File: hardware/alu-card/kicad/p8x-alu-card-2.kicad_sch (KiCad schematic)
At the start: 9 parts, among them U10 74HCT181, U11 74HCT182, U12 74HCT157, U13 74HCT157, U14 74HCT157, U15 74HCT157, U16 74HCT244, U17 FLAGS, U18 74HCT260

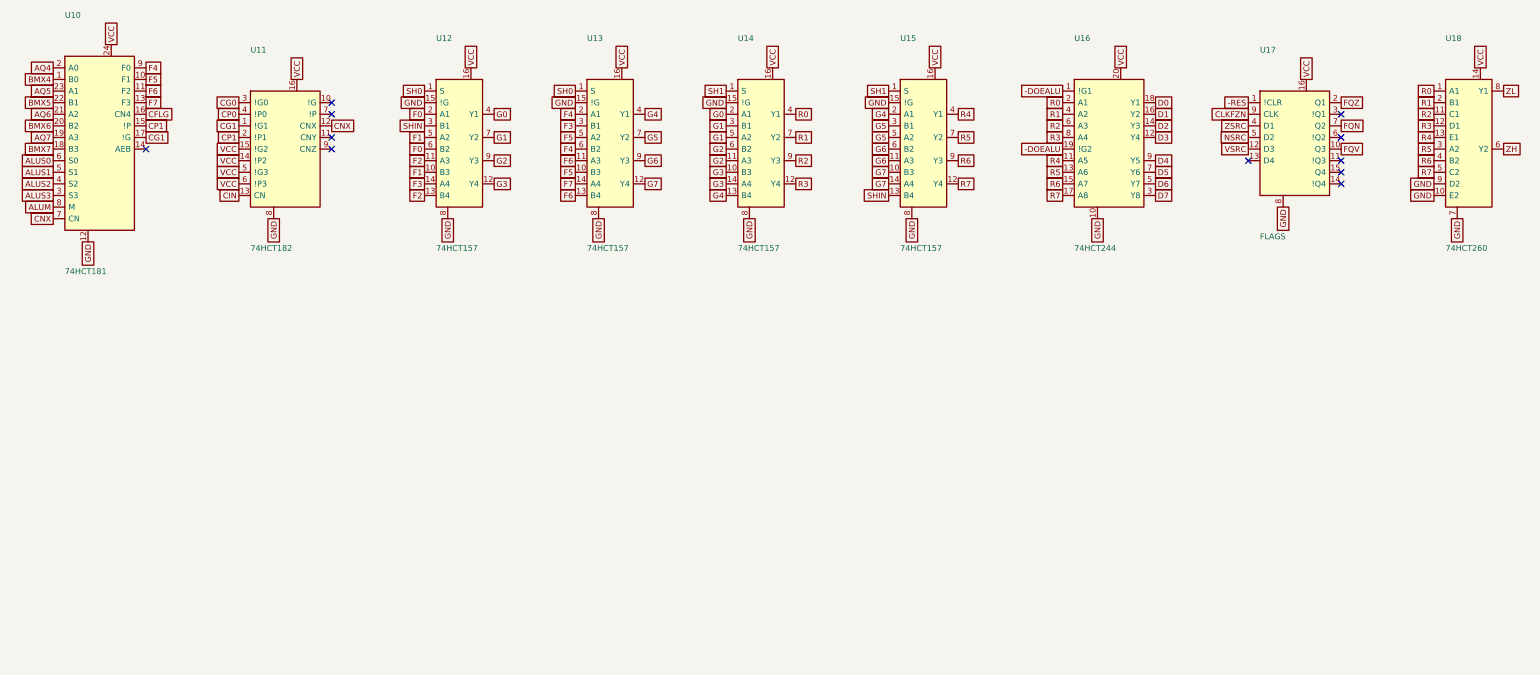
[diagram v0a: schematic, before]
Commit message: feat(sch): draw every P8X card schematic by function
Extend the functional-sheet grouping from the io-card to the control,
regbank, alu, memory, cf, ps2 and bustest cards. functional_sheets now
attaches unnamed glue gates, LEDs, resistors and connectors to the block
they share the most local nets with, so each block lists only its main
parts. A net with two or more pins on a sheet is now wired there even if
it continues elsewhere (its global name label rides on the wire), and
every wire is oriented by drawing side. The regbank gets one pointer per
sheet; the ps2 latches share a sheet with the AVR so the mailbox bus is
drawn. The bustest probe resistors use a straight-order RNISO8DSTR
drawing (the reversed B side forced every wire to cross and the sheet
fell back to labels). build_sch.sh now shows ELK fallbacks and clears old
numbered sheets before a build. All eight netlists match the boards,
ERC 0 errors; the boards change only in footprint link paths.

Co-Authored-By: Claude Opus 5.5 <noreply@anthropic.com>
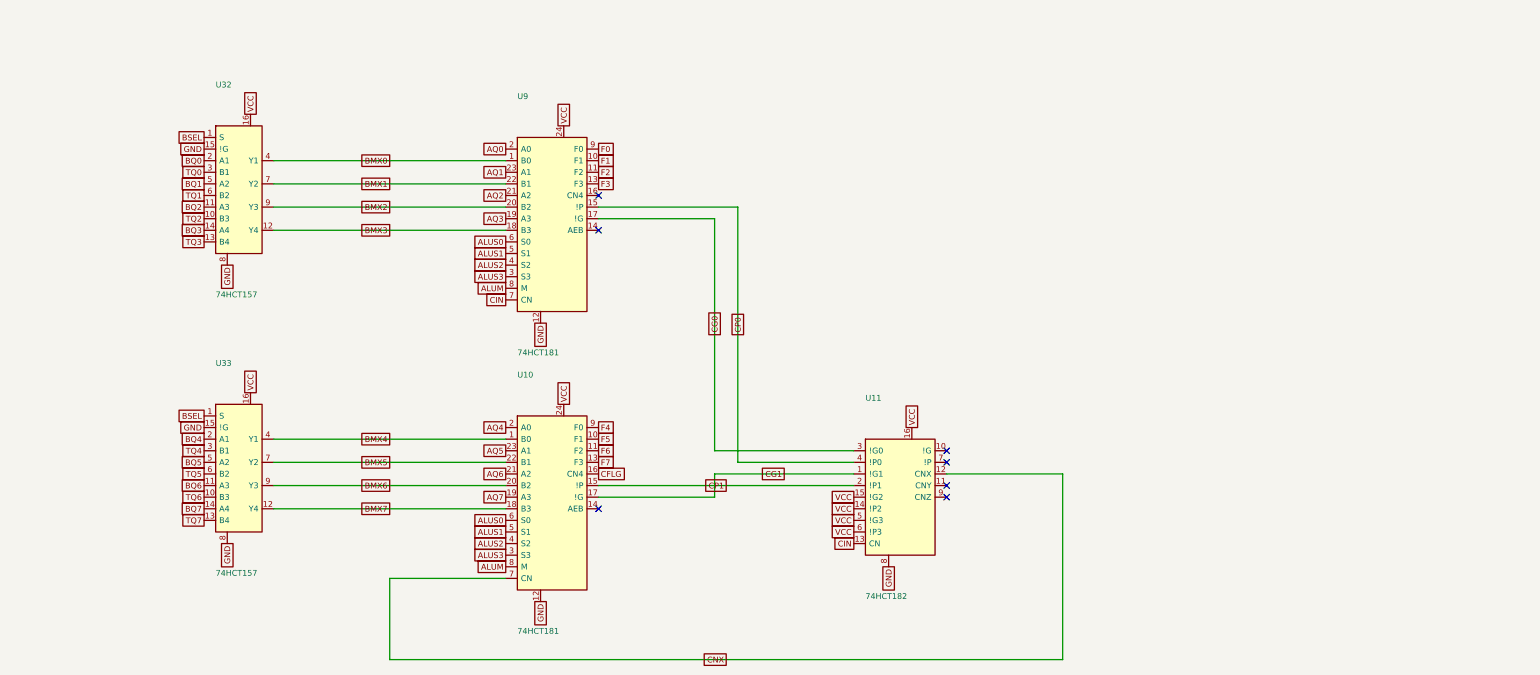
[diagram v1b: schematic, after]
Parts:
- removed U12, U13, U14, U15: 74HCT157, Package_DIP:DIP-16_W7.62mm, symbol p8x:74157
- removed U16: 74HCT244, Package_DIP:DIP-20_W7.62mm, symbol p8x:74244
- removed U17: FLAGS, Package_DIP:DIP-16_W7.62mm, symbol p8x:74175
- removed U18: 74HCT260, Package_DIP:DIP-14_W7.62mm, symbol p8x:74260
- added U32, U33: 74HCT157, Package_DIP:DIP-16_W7.62mm, symbol p8x:74157
- added U9: 74HCT181, Package_DIP:DIP-24_W15.24mm, symbol p8x:74181
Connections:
- net ALUM: now also U9.8 (M)
- net ALUS0: now also U9.6 (S0)
- net ALUS1: now also U9.5 (S1)
- net ALUS2: now also U9.4 (S2)
- net ALUS3: now also U9.3 (S3)
- net BMX4: now also U33.4 (Y1)
- net BMX5: now also U33.7 (Y2)
- net BMX6: now also U33.9 (Y3)
- net BMX7: now also U33.12 (Y4)
- net CG0: now also U9.17 (!G)
- net CIN: now also U9.7 (CN)
- net CP0: now also U9.15 (!P)
- net F0: now also U9.9 (F0)
- net F1: now also U9.10 (F1)
- net F2: now also U9.11 (F2)
- net F3: now also U9.13 (F3)
- net GND: now also U32.15 (!G), U32.8, U33.15 (!G), U33.8, U9.12
- net VCC: now also U32.16, U33.16, U9.24
- new net AQ0: U9.2 (A0)
- new net AQ1: U9.23 (A1)
- new net AQ2: U9.21 (A2)
- new net AQ3: U9.19 (A3)
- new net BMX0: U32.4 (Y1), U9.1 (B0)
- new net BMX1: U32.7 (Y2), U9.22 (B1)
- new net BMX2: U32.9 (Y3), U9.20 (B2)
- new net BMX3: U32.12 (Y4), U9.18 (B3)
- new net BQ0: U32.2 (A1)
- new net BQ1: U32.5 (A2)
- new net BQ2: U32.11 (A3)
- new net BQ3: U32.14 (A4)
- new net BQ4: U33.2 (A1)
- new net BQ5: U33.5 (A2)
- new net BQ6: U33.11 (A3)
- new net BQ7: U33.14 (A4)
- new net BSEL: U32.1 (S), U33.1 (S)
- new net TQ0: U32.3 (B1)
- new net TQ1: U32.6 (B2)
- new net TQ2: U32.10 (B3)
- new net TQ3: U32.13 (B4)
- new net TQ4: U33.3 (B1)
- new net TQ5: U33.6 (B2)
- new net TQ6: U33.10 (B3)
- new net TQ7: U33.13 (B4)
- no-connect marks 11 -> 7
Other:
- moved on the sheet: U10, U11
